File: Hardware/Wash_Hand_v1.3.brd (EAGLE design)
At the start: 71.1 x 48.3 mm, 27 parts, among them J1 I2C, J2 ICSP, J3 SPI, J4 INTERRUPT, J5 EXT_VCC, Q1 16.0 Mhz, U1 ATMEGA328P_TQFP

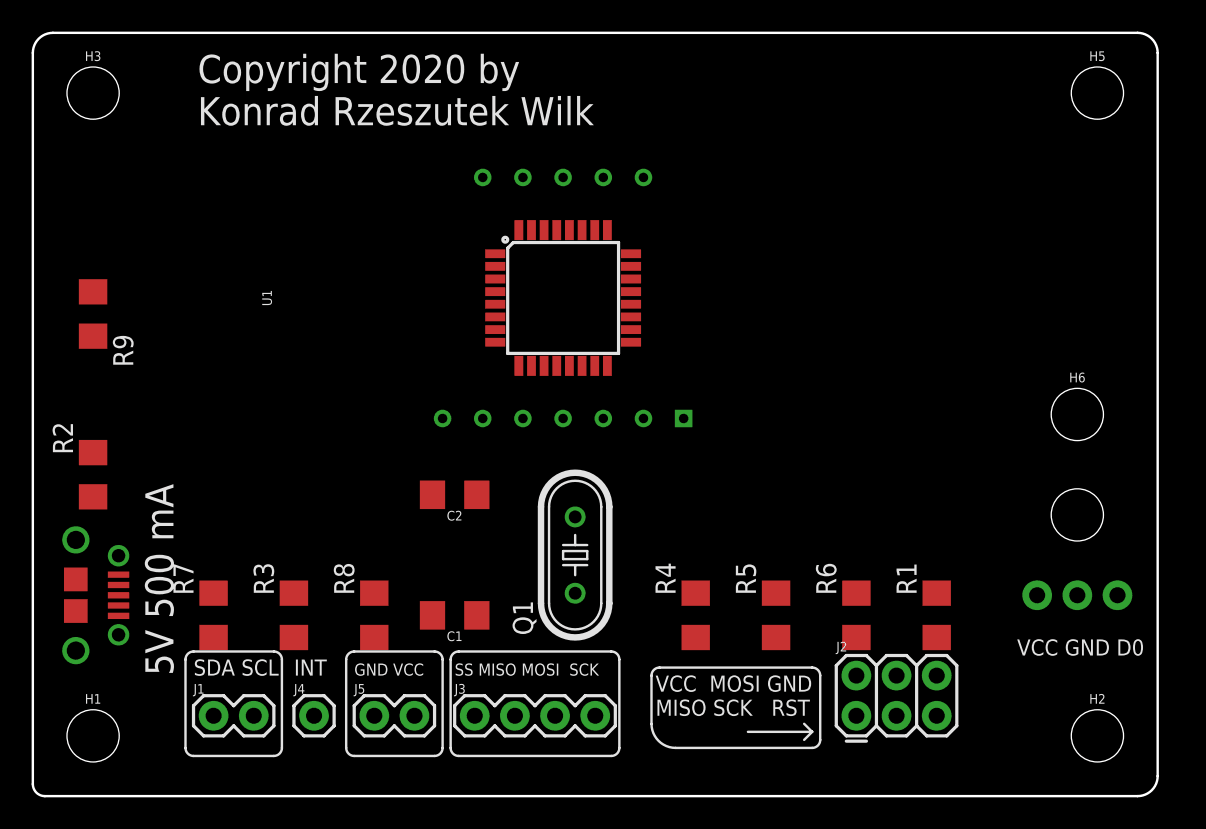
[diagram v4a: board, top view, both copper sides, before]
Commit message: Board: Moved all the SMD components to be behind the 7 Segment LED
(Now that they are SMD they nicely fit behind it).

Signed-off-by: Konrad Rzeszutek Wilk <konrad@darnok.org>
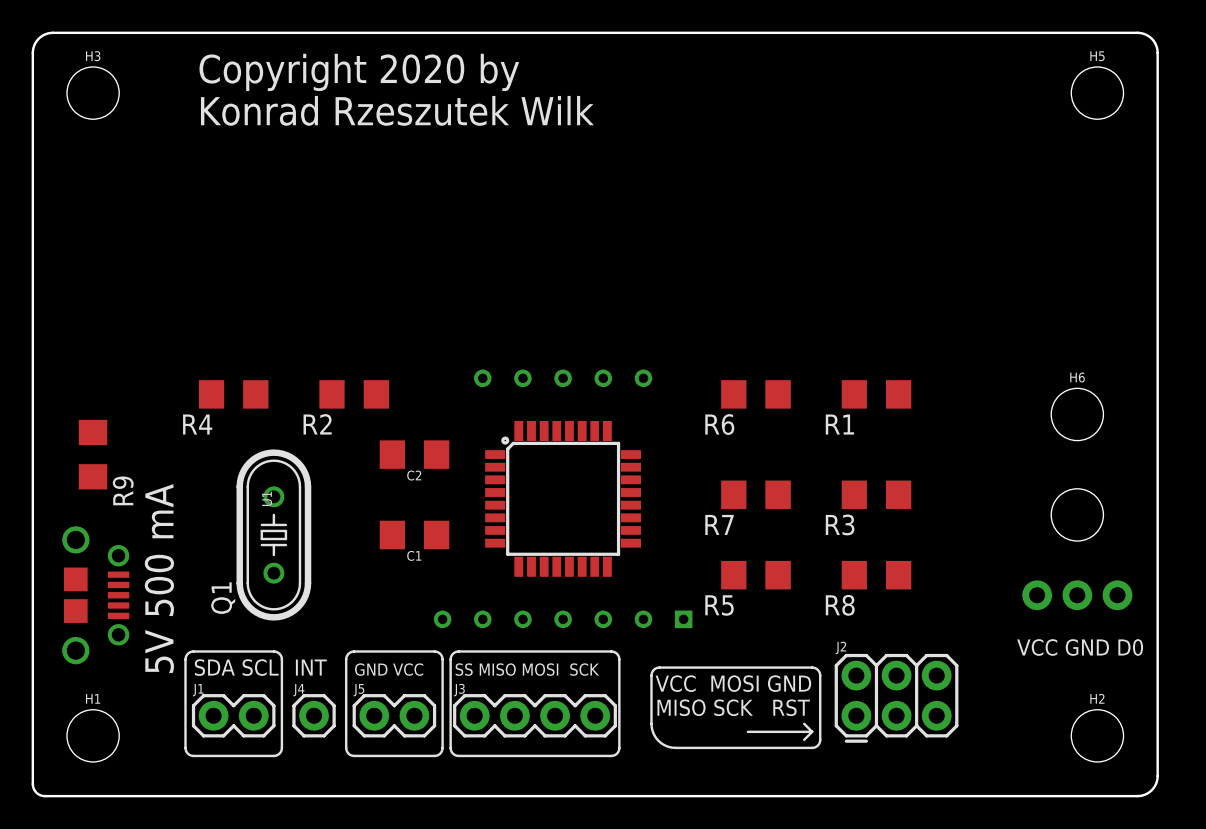
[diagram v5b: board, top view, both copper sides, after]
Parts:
- moved R3 37.6 mm to (53.3, 19.1), turned to 180 degrees
- moved R7 35.1 mm to (45.7, 19.1), turned to 180 degrees
- moved R4 32.4 mm to (12.7, 25.4), turned to 180 degrees
- moved R8 31.9 mm to (53.3, 14.0), turned to 180 degrees
- moved Q1 19.1 mm to (15.2, 16.5)
- moved R2 17.3 mm to (20.3, 25.4), turned to 180 degrees
- moved R6 15.3 mm to (45.7, 25.4), turned to 180 degrees
- moved R1 14.5 mm to (53.3, 25.4), turned to 180 degrees
- moved U$5 12.7 mm to (33.5, 18.8)
- moved U1 12.7 mm to (33.5, 18.8)
- moved R9 8.89 mm to (3.81, 21.6)
- moved C1 5.68 mm to (24.1, 16.5)
- moved C2 3.59 mm to (24.1, 21.6)
- moved R5 2.84 mm to (45.7, 14.0), turned to 180 degrees

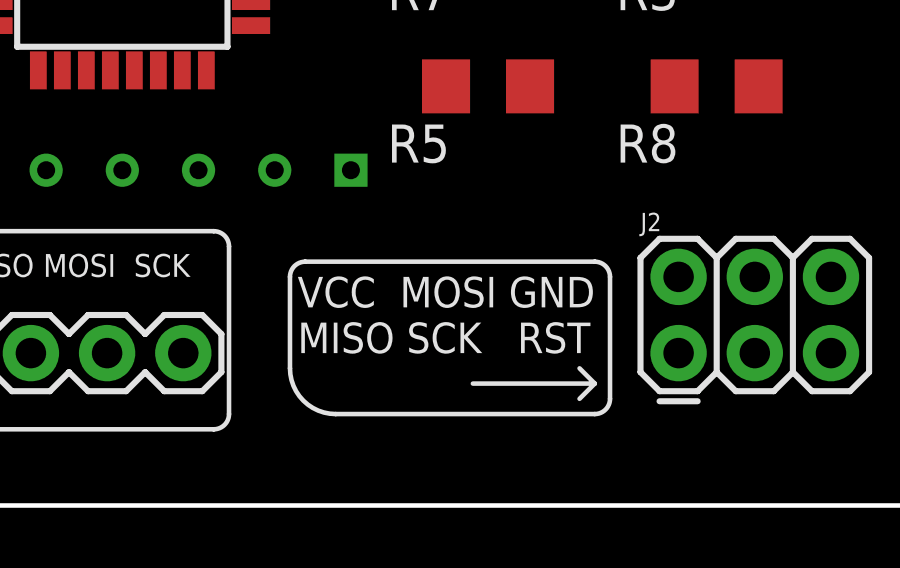
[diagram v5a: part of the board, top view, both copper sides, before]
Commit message: Hardware: Add resistors (4.7K) for the I2C along with a pad.
The pad is there in case we don't want to use the pull-up
resistors.

Signed-off-by: Konrad Rzeszutek Wilk <konrad@darnok.org>
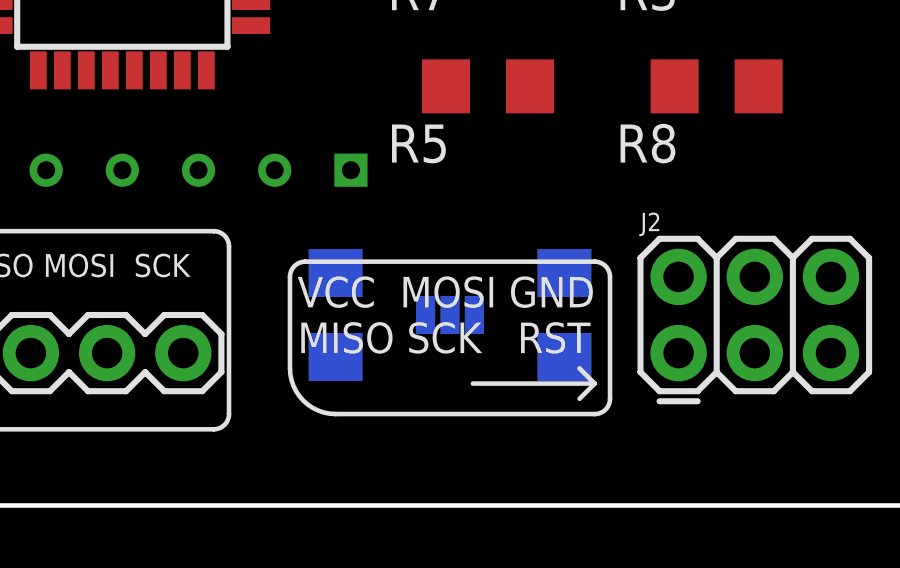
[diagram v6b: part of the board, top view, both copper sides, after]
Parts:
- added JP1: NC, SparkFun-Jumpers:SMT-JUMPER_3_2-NC_PASTE_SILK
- added U$1, U$3: 4.7K, darnok_common:1206
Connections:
- new net N$5: JP1.3, U$3.1
- new net N$6: JP1.1, U$1.2
- net SCL: now also U$1.1
- net SDA: now also U$3.2
- net VCC: now also JP1.2
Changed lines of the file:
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@@
 <attribute name="VALUE" x="66.04" y="22.098" size="0.6096" layer="27" font="vector" ratio="20" align="top-center"/>
+</element>
+<element name="U$3" library="darnok_common" package="1206" value="4.7K" x="48.26" y="6.35" smashed="yes" rot="MR270">
+<attribute name="NAME" x="47.117" y="6.35" size="0.6096" layer="26" font="vector" ratio="20" rot="MR270" align="bottom-center"/>
+<attribute name="VALUE" x="49.403" y="6.35" size="0.6096" layer="28" font="vector" ratio="20" rot="MR270" align="top-center"/>
+</element>
+<element name="U$1" library="darnok_common" package="1206" value="4.7K" x="40.64" y="6.35" smashed="yes" rot="MR270">
+<attribute name="NAME" x="39.497" y="6.35" size="0.6096" layer="26" font="vector" ratio="20" rot="MR0" align="bottom-center"/>
+<attribute name="VALUE" x="41.783" y="6.35" size="0.6096" layer="28" font="vector" ratio="20" rot="MR270" align="top-center"/>
+</element>
+<element name="JP1" library="SparkFun-Jumpers" library_urn="urn:adsk.eagle:library:528" package="SMT-JUMPER_3_2-NC_PASTE_SILK" package3d_urn="urn:adsk.eagle:package:39294/1" value="NC" x="44.45" y="6.35" smashed="yes" rot="MR0">
+<attribute name="NAME" x="44.45" y="7.493" size="0.6096" layer="26" font="vector" ratio="20" rot="MR0" align="bottom-center"/>
+<attribute name="VALUE" x="44.45" y="5.207" size="0.6096" layer="28" font="vector" ratio="20" rot="MR0" align="top-center"/>
 </element>
 </elements>
@@
 <contactref element="R9" pad="1"/>
 <contactref element="J2" pad="5"/>
-<wire x1="3.81" y1="22.99" x2="33.128" y2="23.0886" width="0" layer="19" extent="1-1"/>
-<wire x1="57.15" y1="5.08" x2="33.128" y2="23.0886" width="0" layer="19" extent="1-1"/>
+<wire x1="33.128" y1="23.0886" x2="57.15" y2="5.08" width="0" layer="19" extent="1-1"/>
+<wire x1="3.81" y1="22.73" x2="33.128" y2="23.0886" width="0" layer="19" extent="1-1"/>
 </signal>
 <signal name="VCC">
@@
 <contactref element="U1" pad="4"/>
 <contactref element="U1" pad="6"/>
+<contactref element="JP1" pad="2"/>
 <wire x1="52.07" y1="7.62" x2="63.5" y2="12.7" width="0" layer="19" extent="1-1"/>
-<wire x1="37.8206" y1="16.796" x2="52.07" y2="7.62" width="0" layer="19" extent="1-1"/>
+<wire x1="44.45" y1="6.35" x2="52.07" y2="7.62" width="0" layer="19" extent="16-16"/>
+<wire x1="37.8206" y1="16.796" x2="44.45" y2="6.35" width="0" layer="19" extent="1-16"/>
 <wire x1="37.8206" y1="18.396" x2="37.8206" y2="16.796" width="0" layer="19" extent="1-1"/>
 <wire x1="29.2354" y1="19.196" x2="37.8206" y2="18.396" width="0" layer="19" extent="1-1"/>
 <wire x1="29.2354" y1="17.596" x2="29.2354" y2="19.196" width="0" layer="19" extent="1-1"/>
-<wire x1="3.81" y1="20.19" x2="29.2354" y2="17.596" width="0" layer="19" extent="1-1"/>
-<wire x1="5.42" y1="14" x2="3.81" y2="20.19" width="0" layer="19" extent="1-1"/>
-<wire x1="24.13" y1="5.08" x2="5.42" y2="14" width="0" layer="19" extent="1-1"/>
+<wire x1="24.13" y1="5.08" x2="29.2354" y2="17.596" width="0" layer="19" extent="1-1"/>
+<wire x1="5.42" y1="14" x2="24.13" y2="5.08" width="0" layer="19" extent="1-1"/>
+<wire x1="3.81" y1="25.53" x2="5.42" y2="14" width="0" layer="19" extent="1-1"/>
 </signal>
 <signal name="0">
@@
 </signal>
 <signal name="SDA">
+<contactref element="U1" pad="27"/>
 <contactref element="J1" pad="1"/>
-<contactref element="U1" pad="27"/>
+<contactref element="U$3" pad="2"/>
+<wire x1="48.26" y1="4.95" x2="34.728" y2="23.0886" width="0" layer="19" extent="1-16"/>
 <wire x1="11.43" y1="5.08" x2="34.728" y2="23.0886" width="0" layer="19" extent="1-1"/>
 </signal>
 <signal name="SCL">
+<contactref element="U1" pad="28"/>
 <contactref element="J1" pad="2"/>
-<contactref element="U1" pad="28"/>
+<contactref element="U$1" pad="1"/>
+<wire x1="40.64" y1="7.75" x2="33.928" y2="23.0886" width="0" layer="19" extent="1-16"/>
 <wire x1="13.97" y1="5.08" x2="33.928" y2="23.0886" width="0" layer="19" extent="1-1"/>
 </signal>
@@
 <wire x1="31.528" y1="14.5034" x2="47.12" y2="19.05" width="0" layer="19" extent="1-1"/>
 </signal>
+<signal name="N$5">
+<contactref element="U$3" pad="1"/>
+<contactref element="JP1" pad="3"/>
+<wire x1="43.6372" y1="6.35" x2="48.26" y2="7.75" width="0" layer="19" extent="16-16"/>
+</signal>
+<signal name="N$6">
+<contactref element="U$1" pad="2"/>
+<contactref element="JP1" pad="1"/>
+<wire x1="40.64" y1="4.95" x2="45.2628" y2="6.35" width="0" layer="19" extent="16-16"/>
+</signal>
 </signals>

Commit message: Board: Move the line sensor connectors down
We still want the pins in case our design is no good.
But the line sensor is 0.99 inch tall so we need to make
sure we have enough space to fit this when the board
becomes smaller.

Signed-off-by: Konrad Rzeszutek Wilk <konrad@darnok.org>
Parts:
- moved H4 3.81 mm to (66.0, 14.0)
- moved H6 3.81 mm to (66.0, 20.3)
- moved J 3.81 mm to (63.5, 8.89)
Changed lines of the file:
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@@
 <text x="39.37" y="5.08" size="1.016" layer="25" ratio="14">VCC  MOSI GND
 MISO SCK   RST</text>
-<text x="62.23" y="8.89" size="1.016" layer="25" ratio="14">VCC GND D0</text>
-<text x="69.85" y="8.89" size="1.016" layer="26" ratio="14" rot="MR0">D0 GND VCC</text>
+<text x="62.23" y="6.35" size="1.016" layer="25" ratio="14">VCC GND D0</text>
+<text x="69.85" y="6.35" size="1.016" layer="26" ratio="14" rot="MR0">D0 GND VCC</text>
 <text x="16.51" y="7.62" size="1.016" layer="25" ratio="14">INT</text>
 <text x="20.32" y="7.62" size="0.762" layer="25" ratio="14">GND VCC</text>
-<dimension x1="66.04" y1="12.7" x2="66.04" y2="17.78" x3="59.69" y3="15.24" textsize="1.778" layer="25" unit="inch"/>
-<dimension x1="66.04" y1="12.7" x2="66.04" y2="24.13" x3="63.5" y3="18.415" textsize="1.778" layer="25" unit="inch"/>
+<dimension x1="66.04" y1="8.89" x2="66.04" y2="13.97" x3="59.69" y3="11.43" textsize="1.778" layer="25" unit="inch"/>
+<dimension x1="66.04" y1="8.89" x2="66.04" y2="20.32" x3="63.5" y3="14.605" textsize="1.778" layer="25" unit="inch"/>
 <wire x1="39.624" y1="8.128" x2="39.116" y2="7.62" width="0.1524" layer="25" curve="90"/>
 <wire x1="39.116" y1="7.62" x2="39.116" y2="4.572" width="0.1524" layer="25"/>
@@
 <attribute name="VALUE" value="10uF" x="24.13" y="22.606" size="0.6096" layer="27" font="vector" ratio="20" rot="R180" align="top-center"/>
 </element>
-<element name="J" library="SparkFun-Connectors" library_urn="urn:adsk.eagle:library:513" package="1X03" package3d_urn="urn:adsk.eagle:package:38063/1" value="D0    GND  VCC  ," x="63.5" y="12.7" smashed="yes" rot="MR180">
-<attribute name="NAME" x="62.23" y="11.303" size="0.6096" layer="26" font="vector" ratio="20" rot="MR180"/>
-<attribute name="VALUE" x="62.23" y="14.732" size="0.6096" layer="28" font="vector" ratio="20" rot="MR180"/>
+<element name="J" library="SparkFun-Connectors" library_urn="urn:adsk.eagle:library:513" package="1X03" package3d_urn="urn:adsk.eagle:package:38063/1" value="D0    GND  VCC  ," x="63.5" y="8.89" smashed="yes" rot="MR180">
+<attribute name="NAME" x="62.23" y="7.493" size="0.6096" layer="26" font="vector" ratio="20" rot="MR180"/>
+<attribute name="VALUE" x="62.23" y="10.922" size="0.6096" layer="28" font="vector" ratio="20" rot="MR180"/>
 </element>
 <element name="J1" library="SparkFun-Connectors" library_urn="urn:adsk.eagle:library:513" package="1X02" package3d_urn="urn:adsk.eagle:package:38039/1" value="I2C" x="11.43" y="5.08" smashed="yes">
@@
 <attribute name="VALUE" x="3.81" y="41.148" size="0.6096" layer="27" font="vector" ratio="20" align="top-center"/>
 </element>
-<element name="H4" library="SparkFun-Hardware" library_urn="urn:adsk.eagle:library:519" package="STAND-OFF" package3d_urn="urn:adsk.eagle:package:38630/1" value="STAND-OFF" x="66.04" y="17.78" smashed="yes" rot="MR0">
-<attribute name="NAME" x="66.04" y="19.812" size="0.6096" layer="26" font="vector" ratio="20" rot="MR0" align="bottom-center"/>
-<attribute name="VALUE" x="66.04" y="15.748" size="0.6096" layer="28" font="vector" ratio="20" rot="MR0" align="top-center"/>
+<element name="H4" library="SparkFun-Hardware" library_urn="urn:adsk.eagle:library:519" package="STAND-OFF" package3d_urn="urn:adsk.eagle:package:38630/1" value="STAND-OFF" x="66.04" y="13.97" smashed="yes" rot="MR0">
+<attribute name="NAME" x="66.04" y="16.002" size="0.6096" layer="26" font="vector" ratio="20" rot="MR0" align="bottom-center"/>
+<attribute name="VALUE" x="66.04" y="11.938" size="0.6096" layer="28" font="vector" ratio="20" rot="MR0" align="top-center"/>
 </element>
 <element name="H5" library="SparkFun-Hardware" library_urn="urn:adsk.eagle:library:519" package="STAND-OFF" package3d_urn="urn:adsk.eagle:package:38630/1" value="STAND-OFF" x="67.31" y="44.45" smashed="yes">
@@
 <attribute name="VALUE" x="20.32" y="3.048" size="0.6096" layer="27" font="vector" ratio="20"/>
 </element>
-<element name="H6" library="SparkFun-Hardware" library_urn="urn:adsk.eagle:library:519" package="STAND-OFF" package3d_urn="urn:adsk.eagle:package:38630/1" value="STAND-OFF" x="66.04" y="24.13" smashed="yes">
-<attribute name="NAME" x="66.04" y="26.162" size="0.6096" layer="25" font="vector" ratio="20" align="bottom-center"/>
-<attribute name="VALUE" x="66.04" y="22.098" size="0.6096" layer="27" font="vector" ratio="20" align="top-center"/>
+<element name="H6" library="SparkFun-Hardware" library_urn="urn:adsk.eagle:library:519" package="STAND-OFF" package3d_urn="urn:adsk.eagle:package:38630/1" value="STAND-OFF" x="66.04" y="20.32" smashed="yes">
+<attribute name="NAME" x="66.04" y="22.352" size="0.6096" layer="25" font="vector" ratio="20" align="bottom-center"/>
+<attribute name="VALUE" x="66.04" y="18.288" size="0.6096" layer="27" font="vector" ratio="20" align="top-center"/>
 </element>
 <element name="U$3" library="darnok_common" package="1206" value="4.7K" x="48.26" y="6.35" smashed="yes" rot="MR270">
@@
 <contactref element="U1" pad="6"/>
 <contactref element="JP1" pad="2"/>
-<wire x1="52.07" y1="7.62" x2="63.5" y2="12.7" width="0" layer="19" extent="1-1"/>
+<wire x1="52.07" y1="7.62" x2="63.5" y2="8.89" width="0" layer="19" extent="1-1"/>
 <wire x1="44.45" y1="6.35" x2="52.07" y2="7.62" width="0" layer="19" extent="16-16"/>
 <wire x1="37.8206" y1="16.796" x2="44.45" y2="6.35" width="0" layer="19" extent="1-16"/>
@@
 <contactref element="U1" pad="3"/>
 <contactref element="U1" pad="5"/>
-<wire x1="57.15" y1="7.62" x2="66.04" y2="12.7" width="0" layer="19" extent="1-1"/>
+<wire x1="57.15" y1="7.62" x2="66.04" y2="8.89" width="0" layer="19" extent="1-1"/>
 <wire x1="37.8206" y1="19.196" x2="57.15" y2="7.62" width="0" layer="19" extent="1-1"/>
 <wire x1="29.2354" y1="19.996" x2="37.8206" y2="19.196" width="0" layer="19" extent="1-1"/>
@@
 <contactref element="U1" pad="23"/>
 <contactref element="J" pad="3"/>
-<wire x1="37.8206" y1="20.796" x2="68.58" y2="12.7" width="0" layer="19" extent="1-1"/>
+<wire x1="37.8206" y1="20.796" x2="68.58" y2="8.89" width="0" layer="19" extent="1-1"/>
 </signal>
 <signal name="SDA">

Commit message: Hardware: Add OSHW Logo.
Signed-off-by: Konrad Rzeszutek Wilk <konrad@darnok.org>
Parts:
- added LOGO1: OSHW-LOGOM, SparkFun-Aesthetics:OSHW-LOGO-M
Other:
- board text added: "2020-Jul-22"
- board text removed: "2020-Jul-13"
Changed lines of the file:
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@@
 <text x="6.35" y="7.62" size="1.778" layer="26" rot="MR90">5V 500 mA</text>
 <text x="8.89" y="7.62" size="1.778" layer="25" rot="R90">5V 500 mA</text>
-<text x="21.59" y="1.27" size="1.778" layer="26" ratio="14" rot="MR0">2020-Jul-13</text>
+<text x="21.59" y="1.27" size="1.778" layer="26" ratio="14" rot="MR0">2020-Jul-22</text>
 <text x="10.16" y="7.62" size="1.016" layer="25" ratio="12">SDA SCL</text>
 <text x="26.67" y="7.62" size="0.762" layer="25" ratio="14">SS MISO MOSI  SCK</text>
@@
 <attribute name="VALUE" x="44.45" y="5.207" size="0.6096" layer="28" font="vector" ratio="20" rot="MR0" align="top-center"/>
 </element>
+<element name="LOGO1" library="SparkFun-Aesthetics" library_urn="urn:adsk.eagle:library:507" package="OSHW-LOGO-M" package3d_urn="urn:adsk.eagle:package:37126/1" value="OSHW-LOGOM" x="62.23" y="3.81" smashed="yes" rot="MR0"/>
 </elements>
 <signals>
